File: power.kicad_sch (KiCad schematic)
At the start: 7 parts, among them J16 Conn_01x02, U9 AP63205

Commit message: [update] Thinking about audio.
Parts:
- removed J16: Conn_01x02, Connector_AMASS:AMASS_XT30PW-M_1x02_P2.50mm_Horizontal, symbol Connector_Generic:Conn_01x02

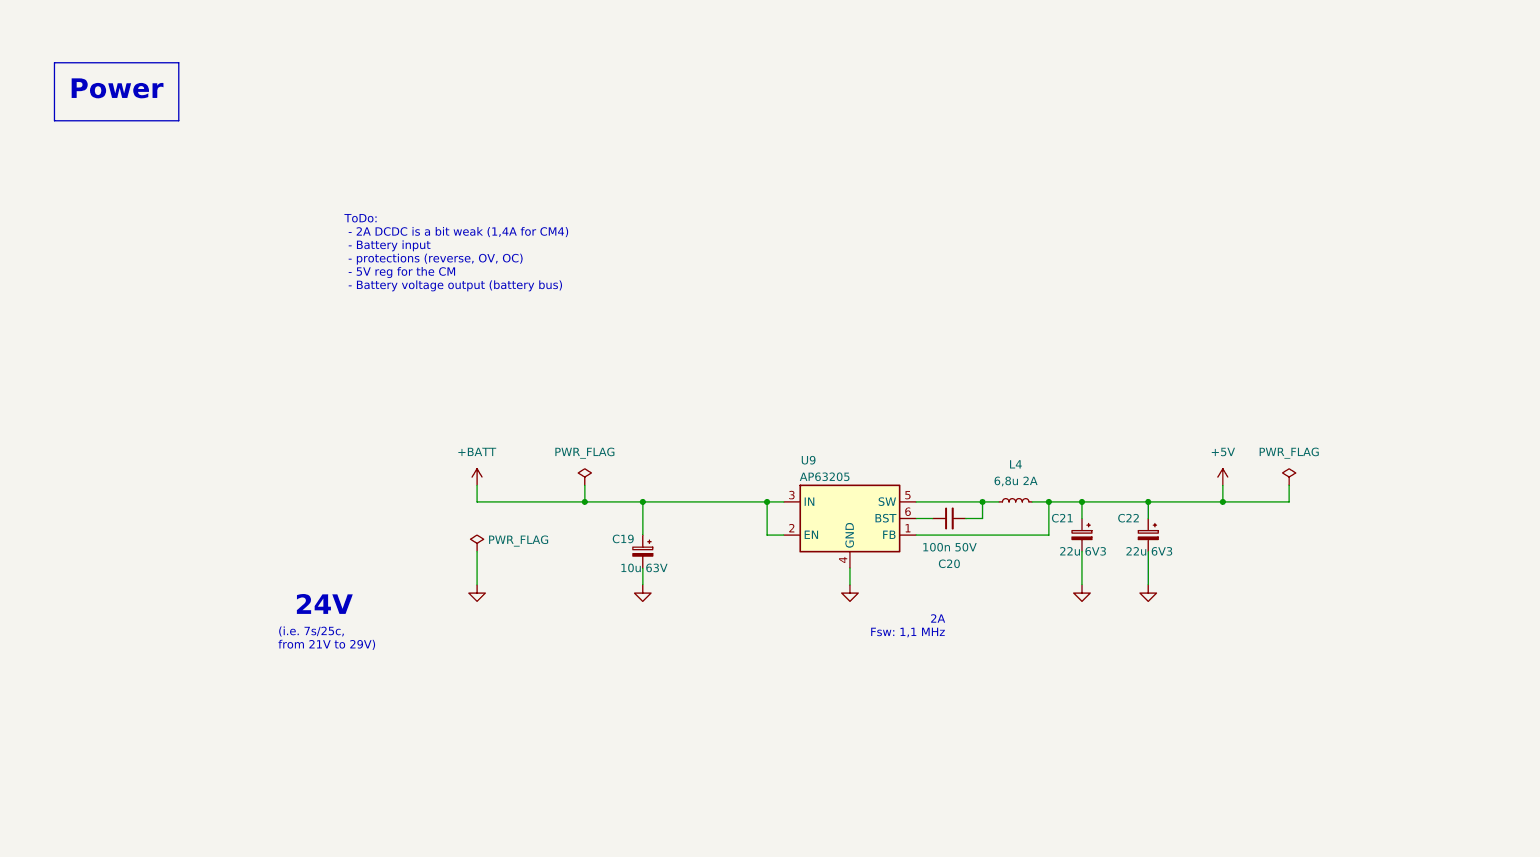
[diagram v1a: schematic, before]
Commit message: [update] BU before changing the 40-pin GPIO
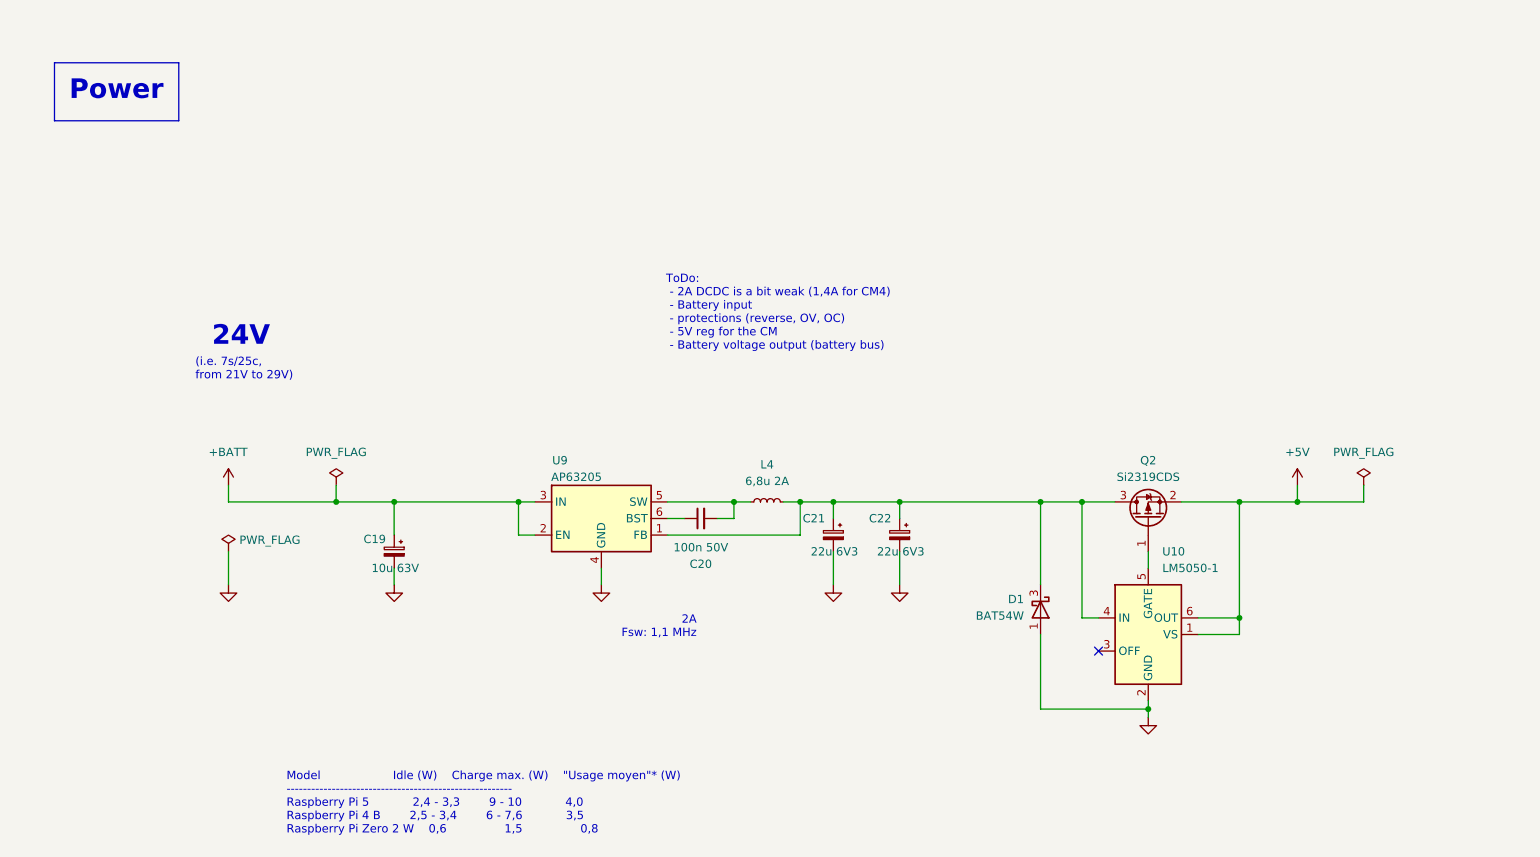
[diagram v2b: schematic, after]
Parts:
- added D1: BAT54W, Package_TO_SOT_SMD:SOT-323_SC-70, symbol Diode:BAT54W
- added Q2: Si2319CDS, Package_TO_SOT_SMD:SOT-23, symbol Transistor_FET:Si2319CDS
- added U10: LM5050-1, Package_TO_SOT_SMD:TSOT-23-6, symbol Power_Management:LM5050-1
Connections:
- net +5V: now also Q2.2 (S), U10.1 (VS), U10.6 (OUT); no longer C21.1, C22.1, L4.1, U9.1 (FB)
- net GND: now also D1.1 (A), U10.2 (GND)
- new net: C21.1, C22.1, D1.3 (K), L4.1, Q2.3 (D), U10.4 (IN), U9.1 (FB)
- new net: Q2.1 (G), U10.5 (GATE)
- no-connect marks 0 -> 1
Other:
- note added: "Model Idle (W) Charge max. (W) "Usage moyen"* (W) ------------------------------------------------------- Raspberry Pi 5 2,4 - 3,3 9 - 10 4,0 Raspberry Pi 4 B 2,5 - 3,4 6 - 7,6 3,5 Raspberry Pi Zero 2 W 0,6 1,5 0,8"
- moved on the sheet: C19, C20, C21, C22, L4, U9

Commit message: [update] Fully routed, need DRC!
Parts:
- U10: LCSC Part (none) -> C473393
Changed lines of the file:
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@@
+			)
+		)
+		(property "LCSC Part" "C473393"
+			(at 198.12 118.11 0)
+			(effects
+				(font
+					(size 1.27 1.27)
+				)
+				(hide yes)
 			)
 		)

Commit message: [update] Release A1, production of 15 boards by JLCPCB
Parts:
- D1: FT Rotation Offset (none) -> 180
- U10: FT Rotation Offset (none) -> 90
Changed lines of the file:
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@@
+			)
+		)
+		(property "FT Rotation Offset" "90"
+			(at 198.12 118.11 0)
+			(effects
+				(font
+					(size 1.27 1.27)
+				)
+				(hide yes)
 			)
 		)
@@
 			(at 181.61 114.3 90)
 			(effects
+				(font
+					(size 1.27 1.27)
+				)
+				(hide yes)
+			)
+		)
+		(property "FT Rotation Offset" "180"
+			(at 181.61 114.3 90)
+			(effects

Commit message: [update] On-going corrections for B1
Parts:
- removed Q2: Si2319CDS, Package_TO_SOT_SMD:SOT-23, symbol Transistor_FET:Si2319CDS
- added C39: 100n 6V3, Capacitor_SMD:C_0402_1005Metric, symbol Device:C_Small
- added Q2: SI2312CDS-T1-GE3, Package_TO_SOT_SMD:TSOT-23, symbol Transistor_FET_Other:Q_NMOS_Depletion_GSD
- added R8: 100R, Resistor_SMD:R_0402_1005Metric, symbol Device:R_Small
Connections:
- net +5V: now also Q2.2 (S), R8.1; no longer U10.1 (VS)
- net GND: now also C39.2
- net at C21.1, C22.1, D1.3 (K)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: now also Q2.3 (D)
- net at U10.5 (GATE): now also Q2.1 (G)
- new net: C39.1, R8.2, U10.1 (VS)
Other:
- note added: "5A"
- moved on the sheet: C21, C22

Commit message: [update] B1-RC1, DRC OK on sch/pcb
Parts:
- added C44: 10n, Capacitor_SMD:C_0402_1005Metric, symbol Device:C_Small
- added D2: 3V3 Zener Diode, Diode_SMD:D_SOD-123, symbol Device:D_Zener
- added R24: 10k, Resistor_SMD:R_0402_1005Metric, symbol Device:R_Small
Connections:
- net +BATT: now also R24.2
- net GND: now also C44.2, D2.2 (A)
- new net IO_06: C44.1, D2.1 (K), R24.1
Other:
- note added: "Switch off detection"
- note removed: "ToDo: - 2A DCDC is a bit weak (1,4A for CM4) - Battery input - protections (reverse, OV, OC) - 5V reg for the CM - Battery voltage output (battery bus)"
- moved on the sheet: C19, C20, C21, C22, C39, D1, L4, Q2, R8, U10, U9

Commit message: [release] B1 (has been produced qtty 125 by JLCPCB)
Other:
- title: RPI Robot Board — CMx Carrier -> elec RPI Robot HAT
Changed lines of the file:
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@@
 	(paper "A4")
 	(title_block
-		(title "RPI Robot Board — CMx Carrier")
-		(date "2026-04-27")
+		(title "elec RPI Robot HAT")
+		(date "2026-05-06")
 		(rev "B1")
 		(company "Pollen Robotics / Hugging Face")
@@
 		(instances
 			(project "elec_RPI_Robot_HAT"
-				(path "/bc05f5da-608c-4912-90e4-36b13d989976/a3937924-4fc8-44c5-a8b9-2db54a98c907"
+				(path "/bc05f5da-608c-4912-90e4-36b13d989976/d25b6afa-8f8a-4256-aaa0-d06d8816c749/1eed69e4-1e3f-4f08-b497-d13d201c1e05"
 					(reference "#PWR099")
 					(unit 1)
@@
 		(instances
 			(project "elec_RPI_Robot_HAT"
-				(path "/bc05f5da-608c-4912-90e4-36b13d989976/a3937924-4fc8-44c5-a8b9-2db54a98c907"
+				(path "/bc05f5da-608c-4912-90e4-36b13d989976/d25b6afa-8f8a-4256-aaa0-d06d8816c749/1eed69e4-1e3f-4f08-b497-d13d201c1e05"
 					(reference "#PWR0102")
 					(unit 1)
@@
 		(instances
 			(project "elec_RPI_Robot_HAT"
-				(path "/bc05f5da-608c-4912-90e4-36b13d989976/a3937924-4fc8-44c5-a8b9-2db54a98c907"
+				(path "/bc05f5da-608c-4912-90e4-36b13d989976/d25b6afa-8f8a-4256-aaa0-d06d8816c749/1eed69e4-1e3f-4f08-b497-d13d201c1e05"
 					(reference "#FLG04")
 					(unit 1)
@@
 		(instances
 			(project "elec_RPI_Robot_HAT"
-				(path "/bc05f5da-608c-4912-90e4-36b13d989976/a3937924-4fc8-44c5-a8b9-2db54a98c907"
+				(path "/bc05f5da-608c-4912-90e4-36b13d989976/d25b6afa-8f8a-4256-aaa0-d06d8816c749/1eed69e4-1e3f-4f08-b497-d13d201c1e05"
 					(reference "U10")
 					(unit 1)
@@
 		(instances
 			(project "elec_RPI_Robot_HAT"
-				(path "/bc05f5da-608c-4912-90e4-36b13d989976/a3937924-4fc8-44c5-a8b9-2db54a98c907"
+				(path "/bc05f5da-608c-4912-90e4-36b13d989976/d25b6afa-8f8a-4256-aaa0-d06d8816c749/1eed69e4-1e3f-4f08-b497-d13d201c1e05"
 					(reference "C19")
 					(unit 1)
@@
 		(instances
 			(project "elec_RPI_Robot_HAT"
-				(path "/bc05f5da-608c-4912-90e4-36b13d989976/a3937924-4fc8-44c5-a8b9-2db54a98c907"
+				(path "/bc05f5da-608c-4912-90e4-36b13d989976/d25b6afa-8f8a-4256-aaa0-d06d8816c749/1eed69e4-1e3f-4f08-b497-d13d201c1e05"
 					(reference "C39")
 					(unit 1)
@@
 		(instances
 			(project "elec_RPI_Robot_HAT"
-				(path "/bc05f5da-608c-4912-90e4-36b13d989976/a3937924-4fc8-44c5-a8b9-2db54a98c907"
+				(path "/bc05f5da-608c-4912-90e4-36b13d989976/d25b6afa-8f8a-4256-aaa0-d06d8816c749/1eed69e4-1e3f-4f08-b497-d13d201c1e05"
 					(reference "#PWR098")
 					(unit 1)
@@
 		(instances
 			(project "elec_RPI_Robot_HAT"
-				(path "/bc05f5da-608c-4912-90e4-36b13d989976/a3937924-4fc8-44c5-a8b9-2db54a98c907"
+				(path "/bc05f5da-608c-4912-90e4-36b13d989976/d25b6afa-8f8a-4256-aaa0-d06d8816c749/1eed69e4-1e3f-4f08-b497-d13d201c1e05"
 					(reference "D1")
 					(unit 1)
@@
 		(instances
 			(project "elec_RPI_Robot_HAT"
-				(path "/bc05f5da-608c-4912-90e4-36b13d989976/a3937924-4fc8-44c5-a8b9-2db54a98c907"
+				(path "/bc05f5da-608c-4912-90e4-36b13d989976/d25b6afa-8f8a-4256-aaa0-d06d8816c749/1eed69e4-1e3f-4f08-b497-d13d201c1e05"
 					(reference "D2")
 					(unit 1)
@@
 		(instances
 			(project "elec_RPI_Robot_HAT"
-				(path "/bc05f5da-608c-4912-90e4-36b13d989976/a3937924-4fc8-44c5-a8b9-2db54a98c907"
+				(path "/bc05f5da-608c-4912-90e4-36b13d989976/d25b6afa-8f8a-4256-aaa0-d06d8816c749/1eed69e4-1e3f-4f08-b497-d13d201c1e05"
 					(reference "#PWR090")
 					(unit 1)
@@
 		(instances
 			(project "elec_RPI_Robot_HAT"
-				(path "/bc05f5da-608c-4912-90e4-36b13d989976/a3937924-4fc8-44c5-a8b9-2db54a98c907"
+				(path "/bc05f5da-608c-4912-90e4-36b13d989976/d25b6afa-8f8a-4256-aaa0-d06d8816c749/1eed69e4-1e3f-4f08-b497-d13d201c1e05"
 					(reference "#FLG02")
 					(unit 1)
@@
 		(instances
 			(project "elec_RPI_Robot_HAT"
-				(path "/bc05f5da-608c-4912-90e4-36b13d989976/a3937924-4fc8-44c5-a8b9-2db54a98c907"
+				(path "/bc05f5da-608c-4912-90e4-36b13d989976/d25b6afa-8f8a-4256-aaa0-d06d8816c749/1eed69e4-1e3f-4f08-b497-d13d201c1e05"
 					(reference "U9")
 					(unit 1)
@@
 		(instances
 			(project "elec_RPI_Robot_HAT"
-				(path "/bc05f5da-608c-4912-90e4-36b13d989976/a3937924-4fc8-44c5-a8b9-2db54a98c907"
+				(path "/bc05f5da-608c-4912-90e4-36b13d989976/d25b6afa-8f8a-4256-aaa0-d06d8816c749/1eed69e4-1e3f-4f08-b497-d13d201c1e05"
 					(reference "L4")
 					(unit 1)
@@
 		(instances
 			(project "elec_RPI_Robot_HAT"
-				(path "/bc05f5da-608c-4912-90e4-36b13d989976/a3937924-4fc8-44c5-a8b9-2db54a98c907"
+				(path "/bc05f5da-608c-4912-90e4-36b13d989976/d25b6afa-8f8a-4256-aaa0-d06d8816c749/1eed69e4-1e3f-4f08-b497-d13d201c1e05"
 					(reference "C44")
 					(unit 1)
@@
 		(instances
 			(project "elec_RPI_Robot_HAT"
-				(path "/bc05f5da-608c-4912-90e4-36b13d989976/a3937924-4fc8-44c5-a8b9-2db54a98c907"
+				(path "/bc05f5da-608c-4912-90e4-36b13d989976/d25b6afa-8f8a-4256-aaa0-d06d8816c749/1eed69e4-1e3f-4f08-b497-d13d201c1e05"
 					(reference "C22")
 					(unit 1)
@@
 		(instances
 			(project "elec_RPI_Robot_HAT"
-				(path "/bc05f5da-608c-4912-90e4-36b13d989976/a3937924-4fc8-44c5-a8b9-2db54a98c907"
+				(path "/bc05f5da-608c-4912-90e4-36b13d989976/d25b6afa-8f8a-4256-aaa0-d06d8816c749/1eed69e4-1e3f-4f08-b497-d13d201c1e05"
 					(reference "Q2")
 					(unit 1)
@@
 		(instances
 			(project "elec_RPI_Robot_HAT"
-				(path "/bc05f5da-608c-4912-90e4-36b13d989976/a3937924-4fc8-44c5-a8b9-2db54a98c907"
+				(path "/bc05f5da-608c-4912-90e4-36b13d989976/d25b6afa-8f8a-4256-aaa0-d06d8816c749/1eed69e4-1e3f-4f08-b497-d13d201c1e05"
 					(reference "R8")
 					(unit 1)
@@
 		(instances
 			(project "elec_RPI_Robot_HAT"
-				(path "/bc05f5da-608c-4912-90e4-36b13d989976/a3937924-4fc8-44c5-a8b9-2db54a98c907"
+				(path "/bc05f5da-608c-4912-90e4-36b13d989976/d25b6afa-8f8a-4256-aaa0-d06d8816c749/1eed69e4-1e3f-4f08-b497-d13d201c1e05"
 					(reference "#PWR0100")
 					(unit 1)
@@
 		(instances
 			(project "elec_RPI_Robot_HAT"
-				(path "/bc05f5da-608c-4912-90e4-36b13d989976/a3937924-4fc8-44c5-a8b9-2db54a98c907"
+				(path "/bc05f5da-608c-4912-90e4-36b13d989976/d25b6afa-8f8a-4256-aaa0-d06d8816c749/1eed69e4-1e3f-4f08-b497-d13d201c1e05"
 					(reference "R24")
 					(unit 1)
@@
 		(instances
 			(project "elec_RPI_Robot_HAT"
-				(path "/bc05f5da-608c-4912-90e4-36b13d989976/a3937924-4fc8-44c5-a8b9-2db54a98c907"
+				(path "/bc05f5da-608c-4912-90e4-36b13d989976/d25b6afa-8f8a-4256-aaa0-d06d8816c749/1eed69e4-1e3f-4f08-b497-d13d201c1e05"
 					(reference "#PWR097")
 					(unit 1)
@@
 		(instances
 			(project "elec_RPI_Robot_HAT"
-				(path "/bc05f5da-608c-4912-90e4-36b13d989976/a3937924-4fc8-44c5-a8b9-2db54a98c907"
+				(path "/bc05f5da-608c-4912-90e4-36b13d989976/d25b6afa-8f8a-4256-aaa0-d06d8816c749/1eed69e4-1e3f-4f08-b497-d13d201c1e05"
 					(reference "#PWR0101")
 					(unit 1)
@@
 		(instances
 			(project "elec_RPI_Robot_HAT"
-				(path "/bc05f5da-608c-4912-90e4-36b13d989976/a3937924-4fc8-44c5-a8b9-2db54a98c907"
+				(path "/bc05f5da-608c-4912-90e4-36b13d989976/d25b6afa-8f8a-4256-aaa0-d06d8816c749/1eed69e4-1e3f-4f08-b497-d13d201c1e05"
 					(reference "#PWR028")
 					(unit 1)
@@
 		(instances
 			(project "elec_RPI_Robot_HAT"
-				(path "/bc05f5da-608c-4912-90e4-36b13d989976/a3937924-4fc8-44c5-a8b9-2db54a98c907"
+				(path "/bc05f5da-608c-4912-90e4-36b13d989976/d25b6afa-8f8a-4256-aaa0-d06d8816c749/1eed69e4-1e3f-4f08-b497-d13d201c1e05"
 					(reference "C20")
 					(unit 1)
@@
 		(instances
 			(project "elec_RPI_Robot_HAT"
-				(path "/bc05f5da-608c-4912-90e4-36b13d989976/a3937924-4fc8-44c5-a8b9-2db54a98c907"
+				(path "/bc05f5da-608c-4912-90e4-36b13d989976/d25b6afa-8f8a-4256-aaa0-d06d8816c749/1eed69e4-1e3f-4f08-b497-d13d201c1e05"
 					(reference "#PWR0103")
 					(unit 1)
@@
 		(instances
 			(project "elec_RPI_Robot_HAT"
-				(path "/bc05f5da-608c-4912-90e4-36b13d989976/a3937924-4fc8-44c5-a8b9-2db54a98c907"
+				(path "/bc05f5da-608c-4912-90e4-36b13d989976/d25b6afa-8f8a-4256-aaa0-d06d8816c749/1eed69e4-1e3f-4f08-b497-d13d201c1e05"
 					(reference "#FLG03")
 					(unit 1)
@@
 		(instances
 			(project "elec_RPI_Robot_HAT"
-				(path "/bc05f5da-608c-4912-90e4-36b13d989976/a3937924-4fc8-44c5-a8b9-2db54a98c907"
+				(path "/bc05f5da-608c-4912-90e4-36b13d989976/d25b6afa-8f8a-4256-aaa0-d06d8816c749/1eed69e4-1e3f-4f08-b497-d13d201c1e05"
 					(reference "C21")
 					(unit 1)
@@
 		(instances
 			(project "elec_RPI_Robot_HAT"
-				(path "/bc05f5da-608c-4912-90e4-36b13d989976/a3937924-4fc8-44c5-a8b9-2db54a98c907"
+				(path "/bc05f5da-608c-4912-90e4-36b13d989976/d25b6afa-8f8a-4256-aaa0-d06d8816c749/1eed69e4-1e3f-4f08-b497-d13d201c1e05"
 					(reference "#PWR096")
 					(unit 1)
